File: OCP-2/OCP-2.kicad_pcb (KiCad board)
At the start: 2 copper layers, 90 x 100 mm, 176 parts, among them X1 ico*отверстие*М3, X2 ico*отверстие*М3, X3 ico*отверстие*М3, X4 ico*отверстие*М3, X5 ico*LOGO_NIKITOS_10х10

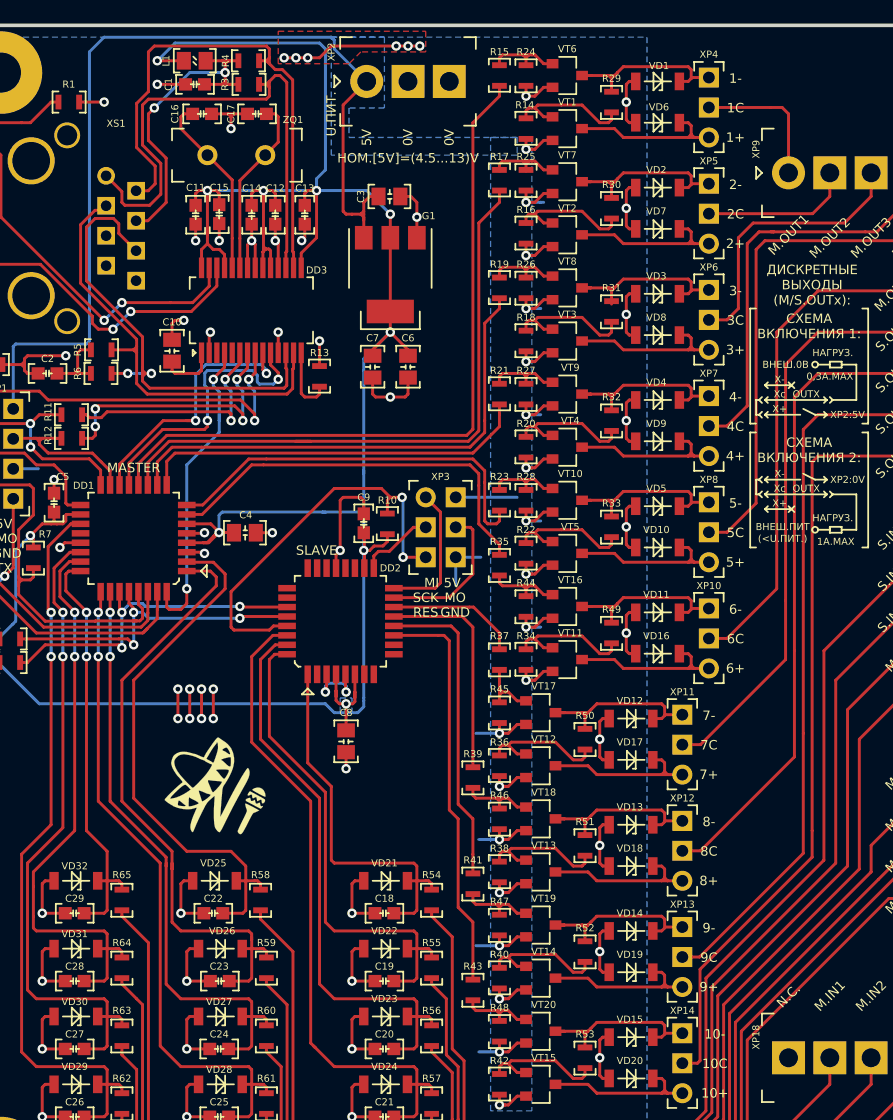
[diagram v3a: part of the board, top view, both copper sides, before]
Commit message: добавлены запирающие диоды в npn канал, обновлен step
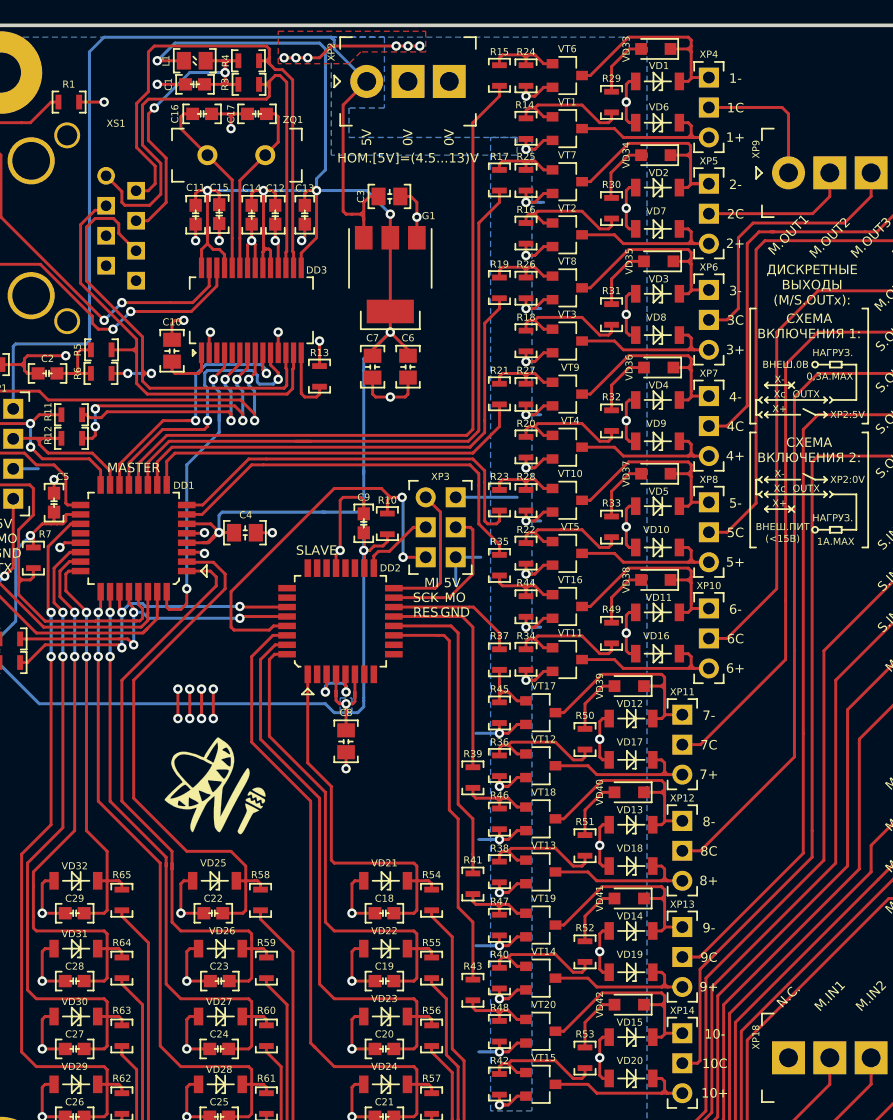
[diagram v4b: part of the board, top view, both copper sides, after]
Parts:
- added VD33: Диод*75В*0,2А*SOD-323, N_VD_HL:D_SOD-323_HandSoldering, F.Cu at (109.5, 52.0)
- added VD34: Диод*75В*0,2А*SOD-323, N_VD_HL:D_SOD-323_HandSoldering, F.Cu at (109.5, 61.0)
- added VD35: Диод*75В*0,2А*SOD-323, N_VD_HL:D_SOD-323_HandSoldering, F.Cu at (109.8, 70.0)
- added VD36: Диод*75В*0,2А*SOD-323, N_VD_HL:D_SOD-323_HandSoldering, F.Cu at (109.8, 79.0)
- added VD37: Диод*75В*0,2А*SOD-323, N_VD_HL:D_SOD-323_HandSoldering, F.Cu at (109.5, 88.0)
- added VD38: Диод*75В*0,2А*SOD-323, N_VD_HL:D_SOD-323_HandSoldering, F.Cu at (109.5, 97.0)
- added VD39: Диод*75В*0,2А*SOD-323, N_VD_HL:D_SOD-323_HandSoldering, F.Cu at (107.2, 106.0)
- added VD40: Диод*75В*0,2А*SOD-323, N_VD_HL:D_SOD-323_HandSoldering, F.Cu at (107.2, 115.0)
- added VD41: Диод*75В*0,2А*SOD-323, N_VD_HL:D_SOD-323_HandSoldering, F.Cu at (107.2, 124.0)
- added VD42: Диод*75В*0,2А*SOD-323, N_VD_HL:D_SOD-323_HandSoldering, F.Cu at (107.2, 133.0)
- moved R31 0.25 mm to (105.8, 74.5)
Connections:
- R29 pad 1: /DOUT1.NPN -> Net-(R29-Pad1)
- R30 pad 1: /DOUT2.NPN -> Net-(R30-Pad1)
- R31 pad 1: /DOUT3.NPN -> Net-(R31-Pad1)
- R32 pad 1: /DOUT4.NPN -> Net-(R32-Pad1)
- R33 pad 1: /DOUT5.NPN -> Net-(R33-Pad1)
- R49 pad 1: /DOUT6.NPN -> Net-(R49-Pad1)
- R50 pad 1: /DOUT7.NPN -> Net-(R50-Pad1)
- R51 pad 1: /DOUT8.NPN -> Net-(R51-Pad1)
- R52 pad 1: /DOUT9.NPN -> Net-(R52-Pad1)
- R53 pad 1: /DOUT10.NPN -> Net-(R53-Pad1)
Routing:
- net /DOUT2.NPN: track 15.0 -> 20.3 mm
- net Net-(R53-Pad1): track 0.00 -> 5.25 mm
- net Net-(R52-Pad1): track 0.00 -> 5.25 mm
- net Net-(R51-Pad1): track 0.00 -> 5.25 mm
- net Net-(R50-Pad1): track 0.00 -> 5.25 mm
- net Net-(R49-Pad1): track 0.00 -> 5.25 mm
- net Net-(R33-Pad1): track 0.00 -> 5.25 mm
- net Net-(R32-Pad1): track 0.00 -> 5.25 mm
- net Net-(R31-Pad1): track 0.00 -> 5.25 mm
- net Net-(R30-Pad1): track 0.00 -> 5.25 mm
- net Net-(R29-Pad1): track 0.00 -> 5.25 mm
- net /DOUT9.NPN: track 15.0 -> 18.7 mm
- net /DOUT8.NPN: track 15.0 -> 18.7 mm
- net /DOUT7.NPN: track 15.0 -> 18.7 mm
- net /DOUT6.NPN: track 15.0 -> 18.7 mm
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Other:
- board text added: "(<15В)"
- board text removed: "(<U.ПИТ.)"
- board text removed: "U.ПИТ."

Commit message: 0А: добавлены диодная защита прог. + стабилитрон на входе питания
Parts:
- added VD1: Диод*75В*0,2А*SOD-323, N_VD_HL:D_SOD-323_HandSoldering, F.Cu at (53.8, 80.2)
- added VD2: Стабилитрон*7,5В*SOD80, N_VD_HL:SOD-80, F.Cu at (89.0, 63.2)
- added VD3: Диод*75В*0,2А*SOD-323, N_VD_HL:D_SOD-323_HandSoldering, F.Cu at (91.8, 87.0)
- moved X5 49.5 mm to (122.2, 113.2)
- moved C5 1.25 mm to (86.0, 65.8)
- moved C6 1.25 mm to (88.5, 79.2)
- moved C7 1.25 mm to (85.5, 79.2)
- moved G1 1.25 mm to (87.0, 72.4)
- moved R2 0.75 mm to (53.2, 78.0)
- moved C2 0.50 mm to (58.5, 79.5)
- moved R5 0.50 mm to (63.0, 77.5)
- moved R6 0.50 mm to (63.0, 79.5)
- moved XP1 0.50 mm to (52.5, 83.0)
- renumbered C4 to C3, C5 to C4, C3 to C5, R16 to R15, R18 to R16, R20 to R17, R22 to R18, R15 to R19, R17 to R20, R19 to R21, R21 to R22, R36 to R35, R38 to R36, R40 to R37, R42 to R38, R35 to R39, R37 to R40, R39 to R41, R41 to R42, VD2 to VD10, VD3 to VD11, VD4 to VD12, VD5 to VD13, VD6 to VD14, VD7 to VD15, VD8 to VD16, VD9 to VD17, VD10 to VD18, VD38 to VD19, VD39 to VD20, VD40 to VD21, VD41 to VD22, VD42 to VD23, VD11 to VD24, VD12 to VD25, VD13 to VD26, VD14 to VD27, VD15 to VD28, VD16 to VD29, VD17 to VD30, VD18 to VD31, VD19 to VD32, VD20 to VD33, VD21 to VD34, VD22 to VD35, VD23 to VD36, VD24 to VD37, VD25 to VD38, VD26 to VD39, VD33 to VD4, VD27 to VD40, VD28 to VD41, VD29 to VD42, VD30 to VD43, VD31 to VD44, VD32 to VD45, VD34 to VD5, VD35 to VD6, VD36 to VD7, VD37 to VD8, VD1 to VD9
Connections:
- C5 pad 1: 5V -> 4...15V
- G1 pad 3: 5V -> 4...15V
- R14 pad 1: 5V -> 4...15V
- R15 pad 1: 5V -> 4...15V
- R16 pad 1: 5V -> 4...15V
- R17 pad 1: 5V -> 4...15V
- R18 pad 1: 5V -> 4...15V
- R34 pad 1: 5V -> 4...15V
- R35 pad 1: 5V -> 4...15V
- R36 pad 1: 5V -> 4...15V
- R37 pad 1: 5V -> 4...15V
- R38 pad 1: 5V -> 4...15V
- VT1 pad 2: 5V -> 4...15V
- VT11 pad 2: 5V -> 4...15V
- VT12 pad 2: 5V -> 4...15V
- VT13 pad 2: 5V -> 4...15V
- VT14 pad 2: 5V -> 4...15V
- VT15 pad 2: 5V -> 4...15V
- VT2 pad 2: 5V -> 4...15V
- VT3 pad 2: 5V -> 4...15V
- VT4 pad 2: 5V -> 4...15V
- VT5 pad 2: 5V -> 4...15V
- XP1 pad 1B: 5V -> /5V.M
- XP2 pad 1: 5V -> 4...15V
- XP3 pad 1B: 5V -> /5V.S
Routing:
- net 4...15V: track 0.00 -> 138.6 mm, vias 0 -> 12
- net 5V: track 126.1 -> 0.00 mm, vias 10 -> 0
- net GND: track 267.2 -> 272.7 mm
- net /5V.S: track 0.00 -> 5.04 mm
- net /5V.M: track 0.00 -> 4.71 mm, vias 0 -> 1
- net 3V3: track 231.1 -> 234.2 mm
- net /MC.OUT3: track 42.6 -> 45.1 mm
- net /MC.OUT6: track 34.4 -> 36.4 mm
- net /MC.OUT5: track 33.9 -> 35.6 mm
- net /MC.OUT2: track 53.4 -> 51.9 mm
- net /ETH.MOSI: track 13.7 -> 12.7 mm
- net Net-(R2-Pad1): track 6.07 -> 5.32 mm
- net /MC.OUT4: track 33.3 -> 32.6 mm
- net /RES.M: track 32.1 -> 31.4 mm
- net /ETH.CLK: track 49.8 -> 49.3 mm
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- added copper zone on B.Cu, net 4...15V
- removed copper zone on B.Cu, net 5V
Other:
- board text added: "(<13В)"
- board text added: "OCP-2-0A.ND"
- board text added: "RDA"
- board text removed: "(<15В)"
